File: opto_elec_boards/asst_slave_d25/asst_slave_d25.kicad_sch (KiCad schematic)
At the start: 36 parts, among them J1 FromMainBoard, J2 PID_Gain_OK, J3 PID_Int_OK, J4 PID_Der_OK, J5 CLOSE, U1 TL084, U2 TL084

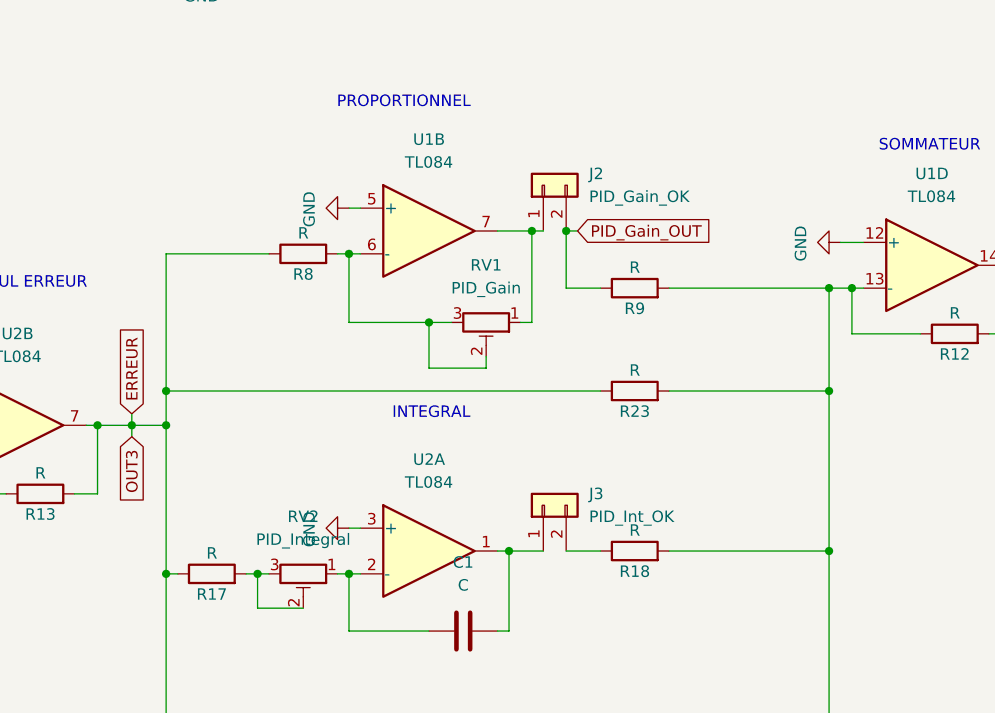
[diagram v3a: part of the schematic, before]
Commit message: Update Opto Boards / Finish Illuminance Control Syst.
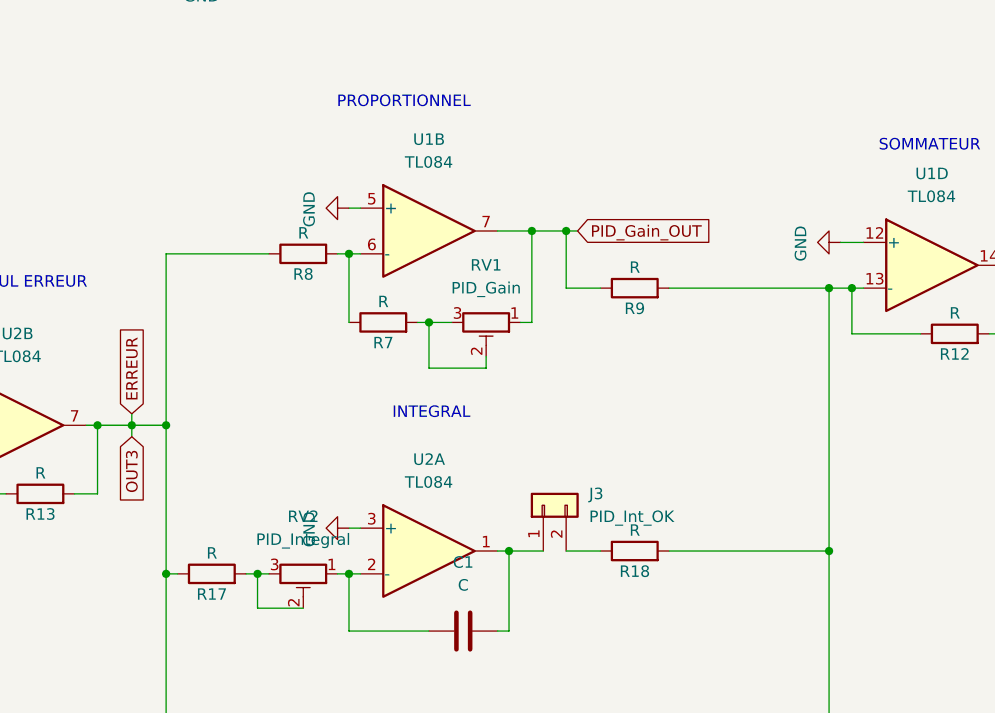
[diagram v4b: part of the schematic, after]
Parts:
- removed J2: PID_Gain_OK, Connector_PinSocket_2.54mm:PinSocket_1x02_P2.54mm_Vertical, symbol Connector_Generic:Conn_01x02
- removed R23: R, Resistor_THT:R_Axial_DIN0207_L6.3mm_D2.5mm_P10.16mm_Horizontal, symbol Device:R
- added R7: R, Resistor_THT:R_Axial_DIN0207_L6.3mm_D2.5mm_P10.16mm_Horizontal, symbol Device:R
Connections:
- net PID_Gain_OUT: now also RV1.1, U1.7
- net at R8.2, U1.6 (-): now also R7.1; no longer RV1.2, RV1.3
- new net: R7.2, RV1.2, RV1.3
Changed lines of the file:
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@@
 	)
 	(junction
-		(at 82.55 97.79)
-		(diameter 0)
-		(color 0 0 0 0)
-	)
-	(junction
 		(at 102.87 118.11)
 		(diameter 0)
@@
 	)
 	(junction
-		(at 111.76 90.17)
-		(diameter 0)
-		(color 0 0 0 0)
-	)
-	(junction
 		(at 66.04 33.02)
 		(diameter 0)
@@
 	)
 	(junction
-		(at 156.21 97.79)
-		(diameter 0)
-		(color 0 0 0 0)
-	)
-	(junction
 		(at 74.93 101.6)
 		(diameter 0)
@@
 	)
 	(junction
-		(at 49.53 44.45)
+		(at 127 80.01)
 		(diameter 0)
 		(color 0 0 0 0)
 	)
 	(junction
-		(at 78.74 101.6)
+		(at 49.53 44.45)
 		(diameter 0)
 		(color 0 0 0 0)
 	)
 	(junction
-		(at 201.93 40.64)
+		(at 78.74 101.6)
 		(diameter 0)
 		(color 0 0 0 0)
 	)
 	(junction
-		(at 127 80.01)
+		(at 201.93 40.64)
 		(diameter 0)
 		(color 0 0 0 0)
@@
 		(color 0 0 0 0)
 	)
+	(junction
+		(at 111.76 90.17)
+		(diameter 0)
+		(color 0 0 0 0)
+	)
 	(wire
 		(pts
@@
 	(wire
 		(pts
-			(xy 102.87 90.17) (xy 111.76 90.17)
-		)
-		(stroke
-			(width 0)
-			(type default)
-		)
-	)
-	(wire
-		(pts
 			(xy 102.87 82.55) (xy 104.14 82.55)
 		)
@@
 	(wire
 		(pts
-			(xy 138.43 97.79) (xy 156.21 97.79)
-		)
-		(stroke
-			(width 0)
-			(type default)
-		)
-	)
-	(wire
-		(pts
 			(xy 196.85 133.35) (xy 196.85 116.84)
 		)
@@
 	(wire
 		(pts
-			(xy 82.55 97.79) (xy 82.55 101.6)
-		)
-		(stroke
-			(width 0)
-			(type default)
-		)
-	)
-	(wire
-		(pts
 			(xy 74.93 101.6) (xy 78.74 101.6)
 		)
@@
 	(wire
 		(pts
-			(xy 130.81 97.79) (xy 82.55 97.79)
-		)
-		(stroke
-			(width 0)
-			(type default)
-		)
-	)
-	(wire
-		(pts
 			(xy 93.98 153.67) (xy 82.55 153.67)
 		)
@@
 	(wire
 		(pts
-			(xy 156.21 115.57) (xy 156.21 97.79)
+			(xy 156.21 86.36) (xy 156.21 115.57)
 		)
 		(stroke
@@
 	(wire
 		(pts
-			(xy 123.19 80.01) (xy 124.46 80.01)
+			(xy 123.19 80.01) (xy 127 80.01)
 		)
 		(stroke
@@
 	(wire
 		(pts
-			(xy 82.55 82.55) (xy 82.55 97.79)
+			(xy 82.55 82.55) (xy 82.55 101.6)
 		)
 		(stroke
@@
 	(wire
 		(pts
-			(xy 156.21 86.36) (xy 156.21 97.79)
-		)
-		(stroke
-			(width 0)
-			(type default)
-		)
-	)
-	(wire
-		(pts
 			(xy 85.09 26.67) (xy 86.36 26.67)
 		)
@@
 	(wire
 		(pts
+			(xy 110.49 90.17) (xy 111.76 90.17)
+		)
+		(stroke
+			(width 0)
+			(type default)
+		)
+	)
+	(wire
+		(pts
 			(xy 138.43 115.57) (xy 156.21 115.57)
 		)
@@
 	)
 	(symbol
+		(lib_id "Device:R")
+		(at 106.68 90.17 90)
+		(unit 1)
+		(exclude_from_sim no)
+		(in_bom yes)
+		(on_board yes)
+		(dnp no)
+		(property "Reference" "R7"
+			(at 106.68 92.456 90)
+			(effects
+				(font
+					(size 1.27 1.27)
+				)
+			)
+		)
+		(property "Value" "R"
+			(at 106.68 87.884 90)
+			(effects
+				(font
+					(size 1.27 1.27)
+				)
+			)
+		)
+		(property "Footprint" "Resistor_THT:R_Axial_DIN0207_L6.3mm_D2.5mm_P10.16mm_Horizontal"
+			(at 106.68 91.948 90)
+			(effects
+				(font
+					(size 1.27 1.27)
+				)
+				(hide yes)
+			)
+		)
+		(property "Datasheet" "~"
+			(at 106.68 90.17 0)
+			(effects
+				(font
+					(size 1.27 1.27)
+				)
+				(hide yes)
+			)
+		)
+		(property "Description" "Resistor"
+			(at 106.68 90.17 0)
+			(effects
+				(font
+					(size 1.27 1.27)
+				)
+				(hide yes)
+			)
+		)
+		(pin "1"
+		)
+		(pin "2"
+		)
+		(instances
+			(project "asst_slave_d25"
+				(path "/57df33c0-6f05-4aba-b5b1-deb15b1b9db6"
+					(reference "R7")
+					(unit 1)
+				)
+			)
+		)
+	)
+	(symbol
 		(lib_id "Amplifier_Operational:TL084")
 		(at 57.15 33.02 0)
@@
 	)
 	(symbol
-		(lib_id "Connector_Generic:Conn_01x02")
-		(at 124.46 74.93 90)
-		(unit 1)
-		(exclude_from_sim no)
-		(in_bom yes)
-		(on_board yes)
-		(dnp no)
-		(fields_autoplaced yes)
-		(property "Reference" "J2"
-			(at 129.54 73.6599 90)
-			(effects
-				(font
-					(size 1.27 1.27)
-				)
-				(justify right)
-			)
-		)
-		(property "Value" "PID_Gain_OK"
-			(at 129.54 76.1999 90)
-			(effects
-				(font
-					(size 1.27 1.27)
-				)
-				(justify right)
-			)
-		)
-		(property "Footprint" "Connector_PinSocket_2.54mm:PinSocket_1x02_P2.54mm_Vertical"
-			(at 124.46 74.93 0)
-			(effects
-				(font
-					(size 1.27 1.27)
-				)
-				(hide yes)
-			)
-		)
-		(property "Datasheet" "~"
-			(at 124.46 74.93 0)
-			(effects
-				(font
-					(size 1.27 1.27)
-				)
-				(hide yes)
-			)
-		)
-		(property "Description" "Generic connector, single row, 01x02, script generated (kicad-library-utils/schlib/autogen/connector/)"
-			(at 124.46 74.93 0)
-			(effects
-				(font
-					(size 1.27 1.27)
-				)
-				(hide yes)
-			)
-		)
-		(pin "1"
-		)
-		(pin "2"
-		)
-		(instances
-			(project ""
-				(path "/57df33c0-6f05-4aba-b5b1-deb15b1b9db6"
-					(reference "J2")
-					(unit 1)
-				)
-			)
-		)
-	)
-	(symbol
 		(lib_id "Device:R")
 		(at 87.63 118.11 90)
@@
 					(unit 1)
 				)
-			)
-		)
-	)
-	(symbol
-		(lib_id "Device:R")
-		(at 134.62 97.79 90)
-		(unit 1)
-		(exclude_from_sim no)
-		(in_bom yes)
-		(on_board yes)
-		(dnp no)
-		(property "Reference" "R23"
-			(at 134.62 100.076 90)
-			(effects
-				(font
-					(size 1.27 1.27)
-				)
-			)
-		)
-		(property "Value" "R"
-			(at 134.62 95.504 90)
-			(effects
-				(font
-					(size 1.27 1.27)
-				)
-			)
-		)
-		(property "Footprint" "Resistor_THT:R_Axial_DIN0207_L6.3mm_D2.5mm_P10.16mm_Horizontal"
-			(at 134.62 99.568 90)
-			(effects
-				(font
-					(size 1.27 1.27)
-				)
-				(hide yes)
-			)
-		)
-		(property "Datasheet" "~"
-			(at 134.62 97.79 0)
-			(effects
-				(font
-					(size 1.27 1.27)
-				)
-				(hide yes)
-			)
-		)
-		(property "Description" "Resistor"
-			(at 134.62 97.79 0)
-			(effects
-				(font
-					(size 1.27 1.27)
-				)
-				(hide yes)
-			)
-		)
-		(pin "1"
-		)
-		(pin "2"
-		)
-		(instances
-			(project "asst_slave_d25"
-				(path "/57df33c0-6f05-4aba-b5b1-deb15b1b9db6"
-					(reference "R23")
-					(unit 1)
-				)
